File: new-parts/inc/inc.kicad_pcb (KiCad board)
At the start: 2 copper layers, 68.6 x 115.6 mm, 20 parts, among them J1 BHR-10-VUA, J2 BHR-10-VUA, J3 Conn_01x02, J4 Conn_01x01, K1 J104D2C12VDC.15S, K2 J104D2C12VDC.15S, K3 J104D2C12VDC.15S, K4 J104D2C12VDC.15S, K5 J104D2C12VDC.15S, K6 J104D2C12VDC.15S, K7 J104D2C12VDC.15S, K8 J104D2C12VDC.15S

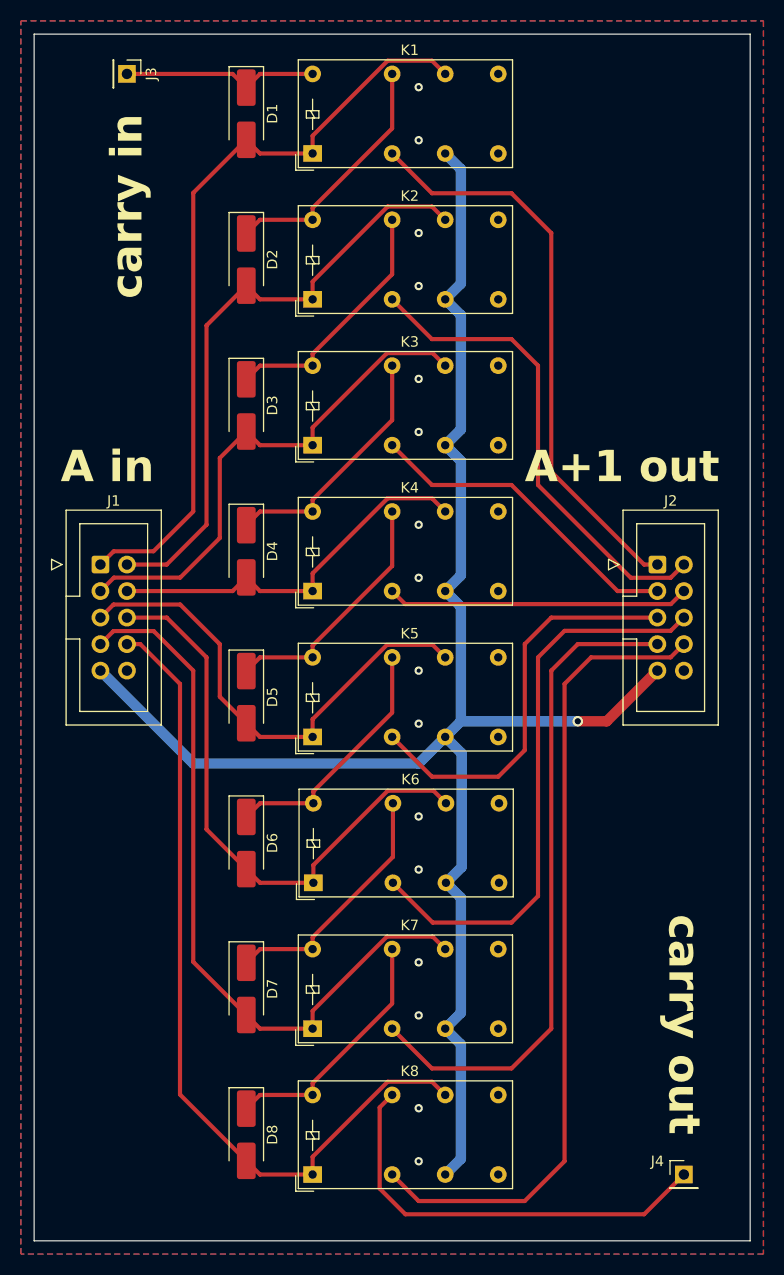
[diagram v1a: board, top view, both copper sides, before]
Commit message: inc: Fix inverted output.
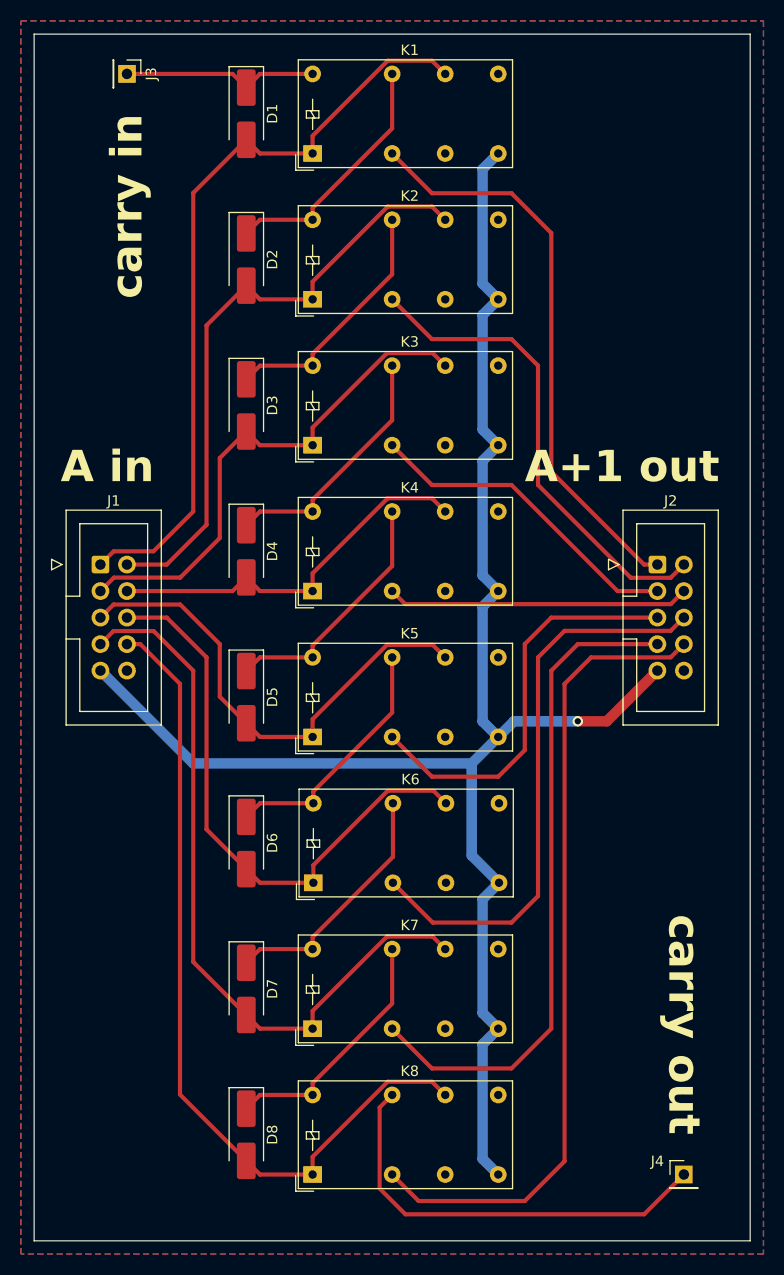
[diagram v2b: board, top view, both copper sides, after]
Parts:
- J3: value Conn_01x02 -> Conn_01x01
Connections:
- K1 pad 12: VCC -> GND
- K1 pad 14: GND -> VCC
- K2 pad 12: VCC -> GND
- K2 pad 14: GND -> VCC
- K3 pad 12: VCC -> GND
- K3 pad 14: GND -> VCC
- K4 pad 12: VCC -> GND
- K4 pad 14: GND -> VCC
- K5 pad 12: VCC -> GND
- K5 pad 14: GND -> VCC
- K6 pad 12: VCC -> GND
- K6 pad 14: GND -> VCC
- K7 pad 12: VCC -> GND
- K7 pad 14: GND -> VCC
- K8 pad 12: VCC -> GND
- K8 pad 14: GND -> VCC
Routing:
- net VCC: track 165.1 -> 164.5 mm
- net GND: vias 16 -> 0

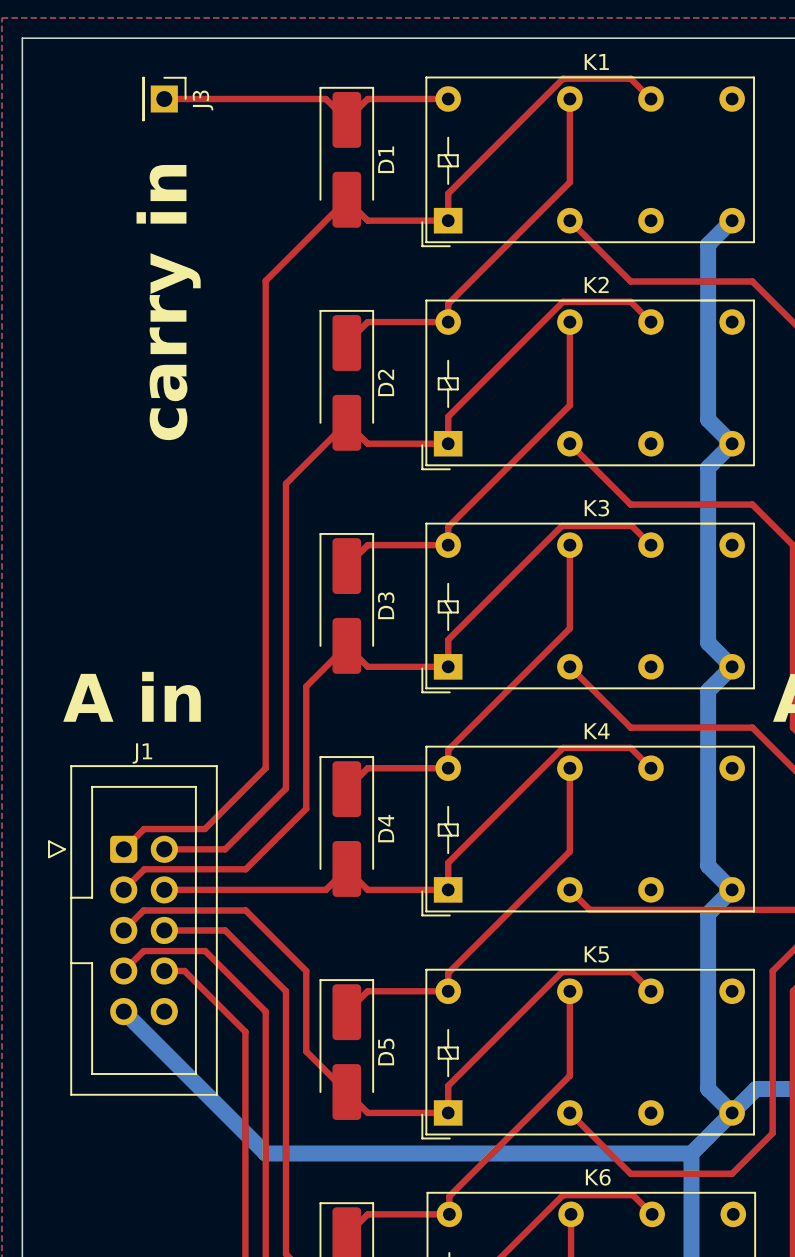
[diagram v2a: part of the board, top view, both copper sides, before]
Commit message: inc: Add solder jumper for stanalone operation (carry in = 1).
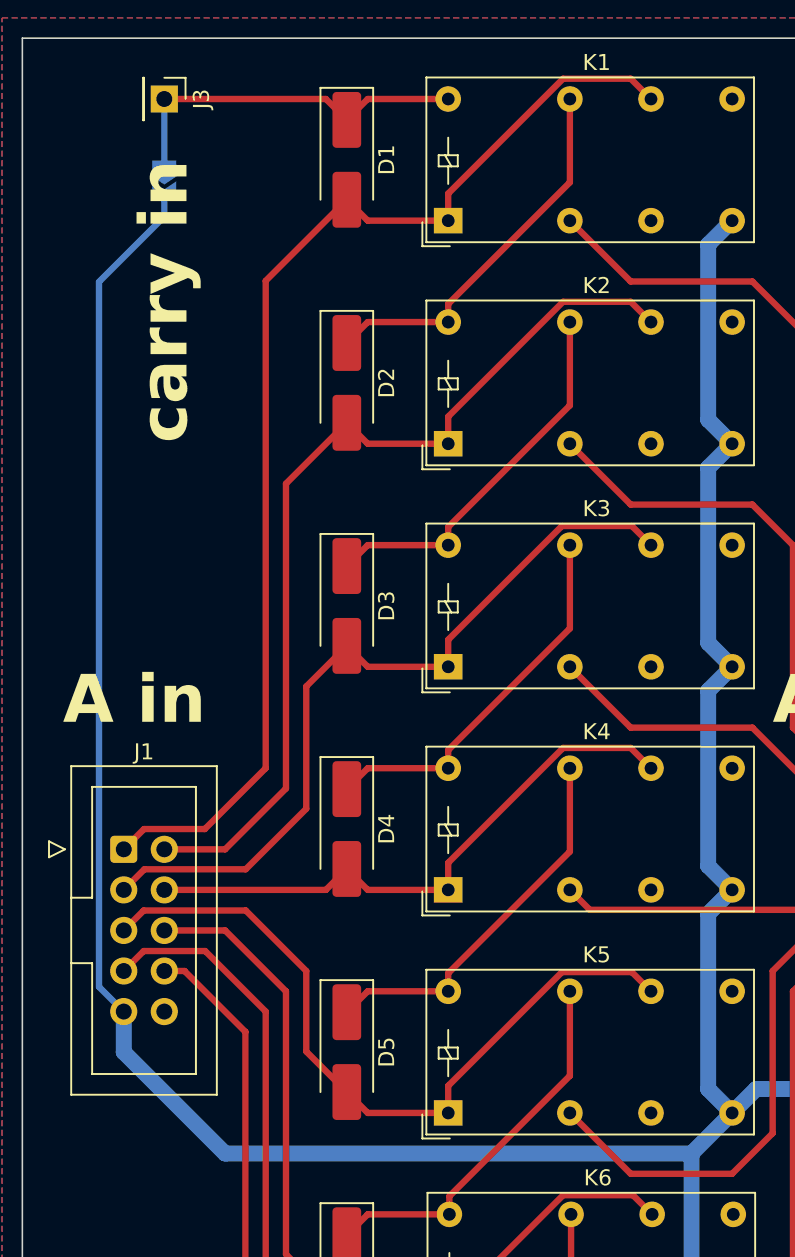
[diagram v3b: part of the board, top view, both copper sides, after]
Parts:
- added JP1: SolderJumper_2_Open, Jumper:SolderJumper-2_P1.3mm_Open_TrianglePad1.0x1.5mm, B.Cu at (125.7, 50.8)
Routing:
- net VCC: track 164.5 -> 219.4 mm
- net Net-(D1-A1): track 18.9 -> 23.2 mm
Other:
- board text added: "close if no carry in"

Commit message: Add "r2" to updated PCBs.
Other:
- board text added: "vis vitalis incrementer r2"
- board text removed: "vis vitalis incrementer"
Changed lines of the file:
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@@
 		)
 	)
-	(gr_text "vis vitalis\nincrementer"
+	(gr_text "vis vitalis\nincrementer r2"
 		(at 172.466 147.32 270)
 		(layer "B.SilkS")
